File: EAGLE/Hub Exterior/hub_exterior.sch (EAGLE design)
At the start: 21 parts, among them Q1 BC337, X2 LLUVIA, X4 GPS, X5 LED_ROJO, X6 BUZZER

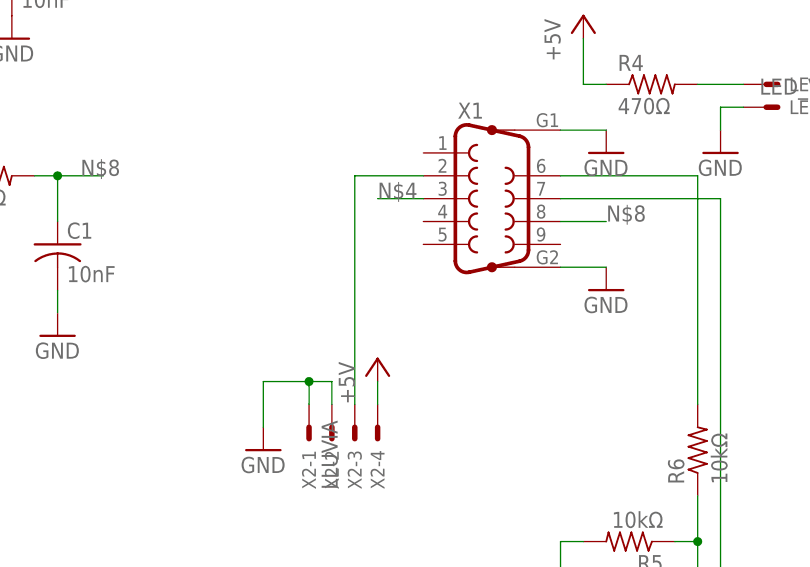
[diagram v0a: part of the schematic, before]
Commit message: Update EAGLE files (hub exterior)
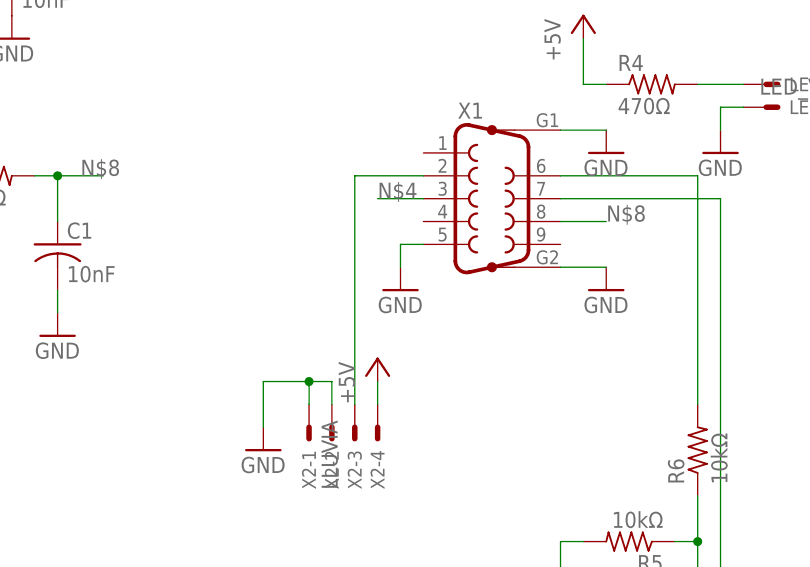
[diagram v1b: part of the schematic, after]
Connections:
- net GND: now also X1.5
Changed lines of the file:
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@@
 <part name="C3" library="rcl" deviceset="CPOL-EU" device="E2.5-5" value="10uF"/>
 <part name="GND11" library="supply1" deviceset="GND" device=""/>
+<part name="GND12" library="supply1" deviceset="GND" device=""/>
 </parts>
 <sheets>
@@
 <instance part="C3" gate="G$1" x="68.58" y="-17.78"/>
 <instance part="GND11" gate="1" x="68.58" y="-25.4"/>
+<instance part="GND12" gate="1" x="12.7" y="22.86"/>
 </instances>
 <busses>
@@
 <pinref part="GND11" gate="1" pin="GND"/>
 </segment>
+<segment>
+<pinref part="X1" gate="G$1" pin="5"/>
+<pinref part="GND12" gate="1" pin="GND"/>
+<wire x1="15.24" y1="27.94" x2="12.7" y2="27.94" width="0.1524" layer="91"/>
+<wire x1="12.7" y1="27.94" x2="12.7" y2="25.4" width="0.1524" layer="91"/>
+</segment>
 </net>
